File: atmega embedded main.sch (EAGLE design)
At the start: 144 parts, among them IC1 ATMEGA328PROUND, K100 SWITCH, K101 SWITCH, K102 SWITCH, K103 SWITCH, K104 SWITCH, K105 SWITCH, K106 SWITCH, K107 SWITCH, K108 SWITCH, K109 SWITCH, K110 SWITCH, K111 SWITCH, K112 SWITCH, K113 SWITCH, K114 SWITCH, K115 SWITCH, K116 SWITCH, K117 SWITCH, K118 SWITCH, K119 SWITCH, K120 SWITCH, K121 SWITCH, K122 SWITCH, K123 SWITCH, K124 SWITCH, K125 SWITCH, K126 SWITCH, K127 SWITCH, K128 SWITCH, K129 SWITCH, K130 SWITCH, K60 SWITCH, K67 SWITCH, K68 SWITCH, K69 SWITCH, K70 SWITCH, K71 SWITCH, K72 SWITCH, K73 SWITCH, K74 SWITCH, K75 SWITCH, K76 SWITCH, K77 SWITCH, K78 SWITCH, K79 SWITCH, K80 SWITCH, K81 SWITCH, K82 SWITCH, K83 SWITCH, K84 SWITCH, K85 SWITCH, K86 SWITCH, K87 SWITCH, K88 SWITCH, K89 SWITCH, K90 SWITCH, K91 SWITCH, K92 SWITCH, K93 SWITCH, K94 SWITCH, K95 SWITCH, K96 SWITCH, K97 SWITCH, K98 SWITCH, K99 SWITCH

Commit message: Compacted stuff around the chip
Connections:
- net N$21: now also IC1.(PCI18/INT0)PD2; no longer IC1.(PCI20/XCK/T0)PD4
- net ROW5: now also IC1.(PCI1/OC1A/OC1S)PB1; no longer IC1.(PCI2/SS/OC1B)PB2
- net ROW6: now also IC1.(PCI2/SS/OC1B)PB2; no longer IC1.(PCI1/OC1A/OC1S)PB1
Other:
- moved on the sheet: R7
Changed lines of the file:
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@@
 <attribute name="VALUE" x="243.84" y="96.774" size="1.778" layer="96"/>
 </instance>
-<instance part="R7" gate="G$1" x="241.3" y="93.98" smashed="yes">
-<attribute name="NAME" x="235.966" y="94.2086" size="1.778" layer="95"/>
-<attribute name="VALUE" x="243.84" y="94.234" size="1.778" layer="96"/>
+<instance part="R7" gate="G$1" x="241.3" y="99.06" smashed="yes">
+<attribute name="NAME" x="235.966" y="99.2886" size="1.778" layer="95"/>
+<attribute name="VALUE" x="243.84" y="99.314" size="1.778" layer="96"/>
 </instance>
 <instance part="K60" gate="G$1" x="68.58" y="35.56" rot="R180"/>
@@
 </segment>
 <segment>
-<pinref part="IC1" gate="G$1" pin="(PCI2/SS/OC1B)PB2"/>
-<wire x1="236.22" y1="76.2" x2="238.76" y2="76.2" width="0.1524" layer="91"/>
-<label x="238.76" y="76.2" size="1.778" layer="95"/>
+<pinref part="IC1" gate="G$1" pin="(PCI1/OC1A/OC1S)PB1"/>
+<wire x1="236.22" y1="78.74" x2="238.76" y2="78.74" width="0.1524" layer="91"/>
+<label x="238.76" y="78.74" size="1.778" layer="95"/>
 </segment>
 </net>
@@
 <segment>
 <pinref part="R7" gate="G$1" pin="2"/>
-<wire x1="246.38" y1="93.98" x2="248.92" y2="93.98" width="0.1524" layer="91"/>
-<label x="248.92" y="93.98" size="1.778" layer="95"/>
+<wire x1="246.38" y1="99.06" x2="248.92" y2="99.06" width="0.1524" layer="91"/>
+<label x="248.92" y="99.06" size="1.778" layer="95"/>
 </segment>
 </net>
@@
 </segment>
 <segment>
-<pinref part="IC1" gate="G$1" pin="(PCI1/OC1A/OC1S)PB1"/>
-<wire x1="236.22" y1="78.74" x2="238.76" y2="78.74" width="0.1524" layer="91"/>
-<label x="238.76" y="78.74" size="1.778" layer="95"/>
+<pinref part="IC1" gate="G$1" pin="(PCI2/SS/OC1B)PB2"/>
+<wire x1="236.22" y1="76.2" x2="238.76" y2="76.2" width="0.1524" layer="91"/>
+<label x="238.76" y="76.2" size="1.778" layer="95"/>
 </segment>
 </net>
@@
 </segment>
 </net>
-<net name="N$21" class="0">
-<segment>
-<pinref part="IC1" gate="G$1" pin="(PCI20/XCK/T0)PD4"/>
-<pinref part="R7" gate="G$1" pin="1"/>
-</segment>
-</net>
 <net name="N$68" class="0">
 <segment>
@@
 </segment>
 </net>
+<net name="N$21" class="0">
+<segment>
+<pinref part="IC1" gate="G$1" pin="(PCI18/INT0)PD2"/>
+<pinref part="R7" gate="G$1" pin="1"/>
+</segment>
+</net>

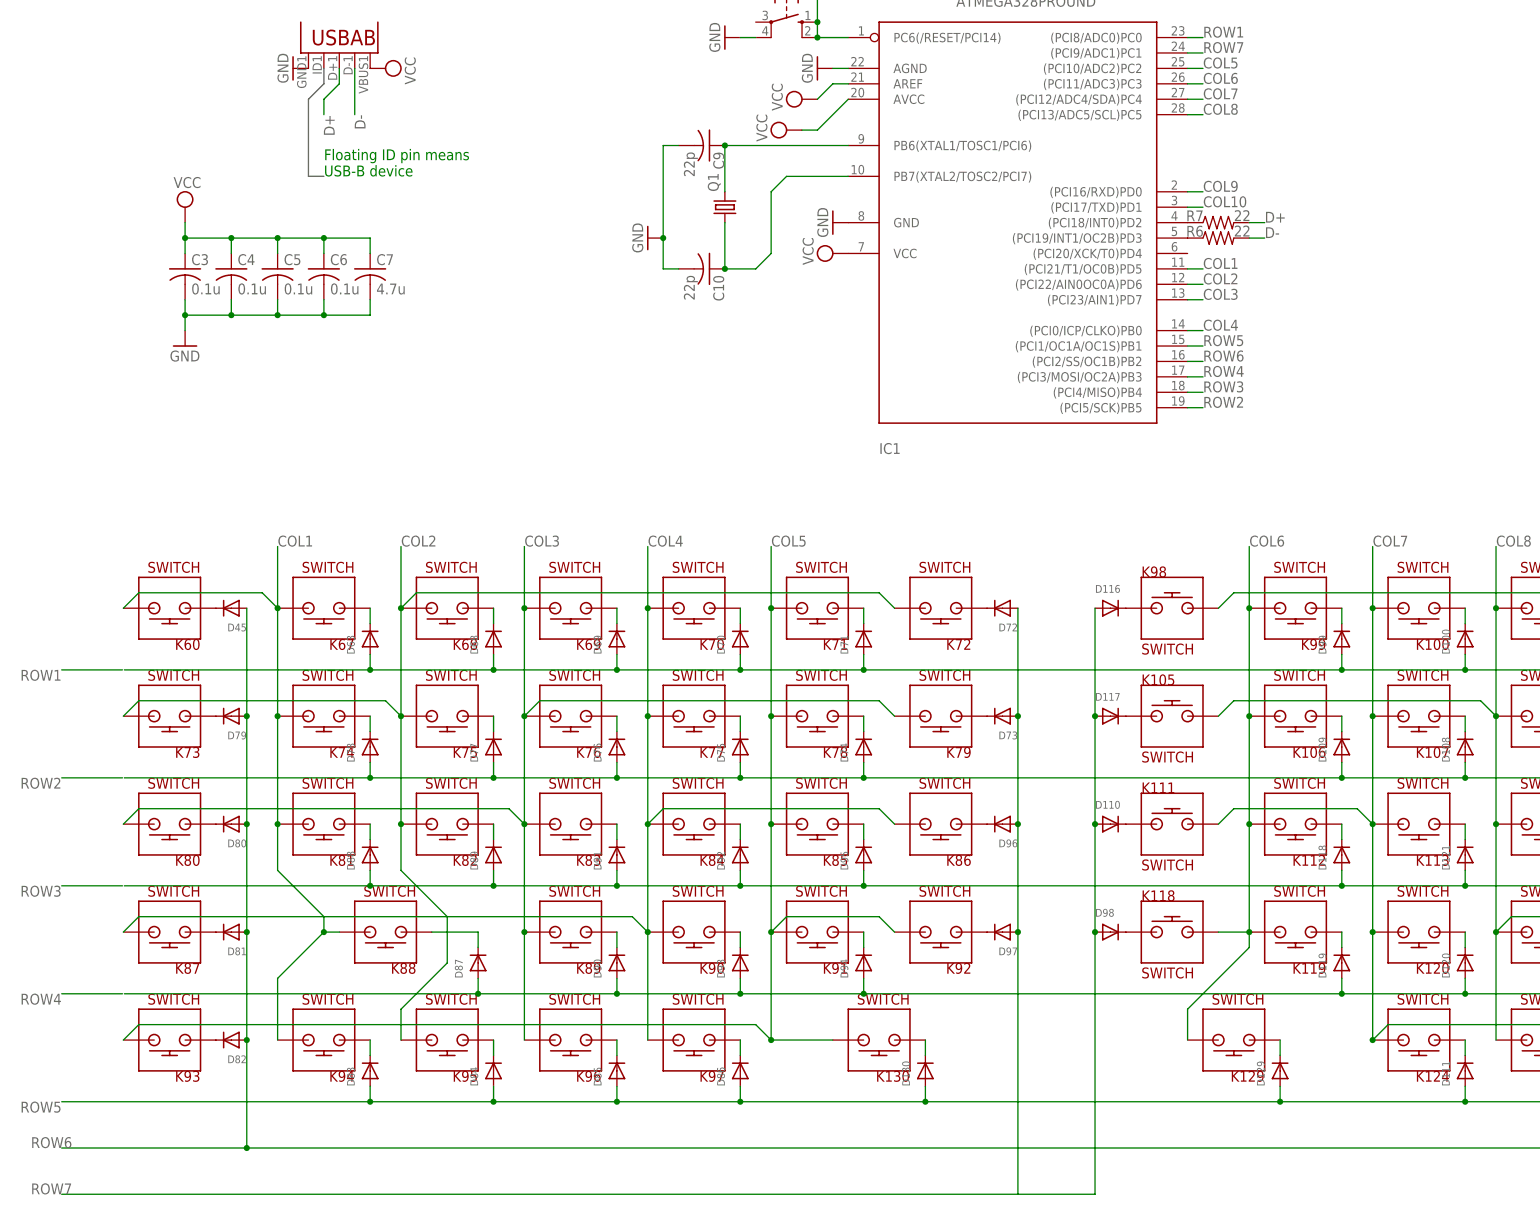
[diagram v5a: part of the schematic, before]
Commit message: Fixed errors and made adjustments for USB
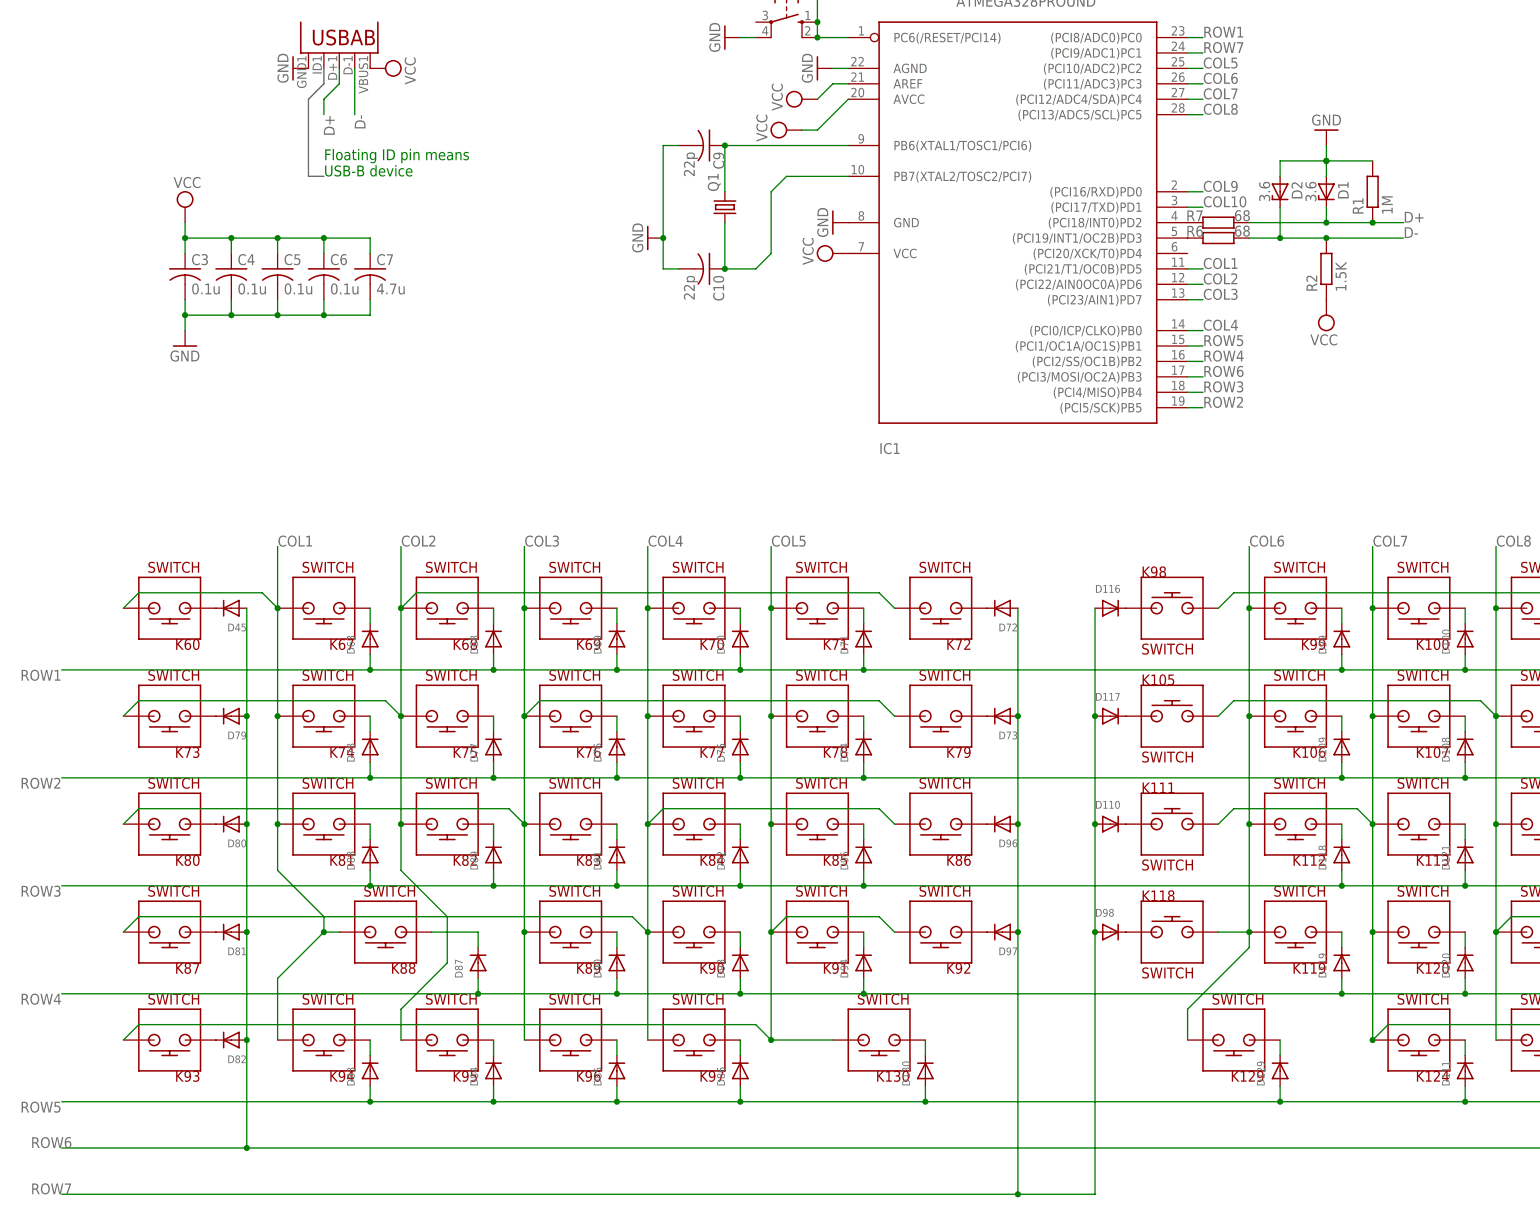
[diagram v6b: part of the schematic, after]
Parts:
- added D1, D2: 3.6, diode:ZENER-DIODESMB
- added R1: 1M, eagle-ltspice:RR1206
- added R2: 1.5K, eagle-ltspice:RR1206
- R6, R7: value 22 -> 68; device adafruit:R-US_M0805 -> eagle-ltspice:RR1206
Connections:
- net D+: now also D1.C, R1.1
- net D-: now also D2.C, R2.2
- net GND: now also D1.A, D2.A, R1.2
- net ROW4: now also IC1.(PCI2/SS/OC1B)PB2; no longer IC1.(PCI3/MOSI/OC2A)PB3
- net ROW6: now also IC1.(PCI3/MOSI/OC2A)PB3; no longer IC1.(PCI2/SS/OC1B)PB2
- net VCC: now also R2.1
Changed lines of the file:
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@@
 <part name="SUPPLY7" library="supply2" library_urn="urn:adsk.eagle:library:372" deviceset="VCC" device=""/>
 <part name="GND10" library="supply1" library_urn="urn:adsk.eagle:library:371" deviceset="GND" device=""/>
-<part name="R6" library="adafruit" deviceset="R-US_" device="M0805" value="22"/>
-<part name="R7" library="adafruit" deviceset="R-US_" device="M0805" value="22"/>
+<part name="R6" library="eagle-ltspice" library_urn="urn:adsk.eagle:library:217" deviceset="R" device="R1206" package3d_urn="urn:adsk.eagle:package:13301/1" value="68"/>
+<part name="R7" library="eagle-ltspice" library_urn="urn:adsk.eagle:library:217" deviceset="R" device="R1206" package3d_urn="urn:adsk.eagle:package:13301/1" value="68"/>
 <part name="K60" library="keyboard_switch" deviceset="SWITCH" device=""/>
 <part name="K67" library="keyboard_switch" deviceset="SWITCH" device=""/>
@@
 <part name="Q1" library="crystal" library_urn="urn:adsk.eagle:library:204" deviceset="CRYSTAL" device="HC49S" package3d_urn="urn:adsk.eagle:package:12071/1"/>
 <part name="S1" library="switch-omron" library_urn="urn:adsk.eagle:library:377" deviceset="10-XX" device="" package3d_urn="urn:adsk.eagle:package:27496/1"/>
+<part name="GND1" library="supply1" library_urn="urn:adsk.eagle:library:371" deviceset="GND" device=""/>
+<part name="D1" library="diode" library_urn="urn:adsk.eagle:library:210" deviceset="ZENER-DIODE" device="SMB" package3d_urn="urn:adsk.eagle:package:43404/2" value="3.6"/>
+<part name="D2" library="diode" library_urn="urn:adsk.eagle:library:210" deviceset="ZENER-DIODE" device="SMB" package3d_urn="urn:adsk.eagle:package:43404/2" value="3.6"/>
+<part name="R1" library="eagle-ltspice" library_urn="urn:adsk.eagle:library:217" deviceset="R" device="R1206" package3d_urn="urn:adsk.eagle:package:13301/1" value="1M"/>
+<part name="SUPPLY2" library="supply2" library_urn="urn:adsk.eagle:library:372" deviceset="VCC" device=""/>
+<part name="R2" library="eagle-ltspice" library_urn="urn:adsk.eagle:library:217" deviceset="R" device="R1206" package3d_urn="urn:adsk.eagle:package:13301/1" value="1.5K"/>
 </parts>
 <sheets>
@@
 <instance part="Q1" gate="G$1" x="160.02" y="101.6" rot="R90"/>
 <instance part="S1" gate="1" x="170.18" y="132.08" rot="R270"/>
+<instance part="GND1" gate="1" x="259.08" y="114.3" rot="R180"/>
+<instance part="D1" gate="G$1" x="259.08" y="104.14" rot="R270"/>
+<instance part="D2" gate="G$1" x="251.46" y="104.14" rot="R270"/>
+<instance part="R1" gate="G$1" x="266.7" y="104.14" rot="R90"/>
+<instance part="SUPPLY2" gate="G$1" x="259.08" y="83.82" rot="R180"/>
+<instance part="R2" gate="G$1" x="259.08" y="91.44" rot="R90"/>
 </instances>
 <busses>
@@
 <pinref part="GNDUSB" gate="1" pin="GND"/>
 </segment>
+<segment>
+<pinref part="D2" gate="G$1" pin="A"/>
+<wire x1="251.46" y1="106.68" x2="251.46" y2="109.22" width="0.1524" layer="91"/>
+<wire x1="251.46" y1="109.22" x2="259.08" y2="109.22" width="0.1524" layer="91"/>
+<pinref part="GND1" gate="1" pin="GND"/>
+<wire x1="259.08" y1="111.76" x2="259.08" y2="109.22" width="0.1524" layer="91"/>
+<pinref part="R1" gate="G$1" pin="2"/>
+<junction x="259.08" y="109.22"/>
+<pinref part="D1" gate="G$1" pin="A"/>
+<wire x1="259.08" y1="109.22" x2="266.7" y2="109.22" width="0.1524" layer="91"/>
+<wire x1="259.08" y1="109.22" x2="259.08" y2="106.68" width="0.1524" layer="91"/>
+<junction x="259.08" y="109.22"/>
+</segment>
 </net>
 <net name="VCC" class="0">
@@
 <pinref part="U1" gate="G$1" pin="VBUS"/>
 <pinref part="VCCUSB" gate="G$1" pin="VCC"/>
+</segment>
+<segment>
+<pinref part="R2" gate="G$1" pin="1"/>
+<pinref part="SUPPLY2" gate="G$1" pin="VCC"/>
 </segment>
 </net>
@@
 <net name="ROW4" class="0">
 <segment>
-<wire x1="50.8" y1="-27.94" x2="60.8076" y2="-27.94" width="0.1524" layer="91"/>
-<label x="50.8" y="-27.94" size="1.778" layer="95" rot="R180"/>
-</segment>
-<segment>
 <pinref part="D94" gate="G$1" pin="A"/>
 <wire x1="162.56" y1="-27.94" x2="182.88" y2="-27.94" width="0.1524" layer="91"/>
@@
 <wire x1="119.38" y1="-25.4" x2="119.38" y2="-27.94" width="0.1524" layer="91"/>
 <junction x="119.38" y="-27.94"/>
-<wire x1="61.1124" y1="-27.94" x2="119.38" y2="-27.94" width="0.1524" layer="91"/>
+<wire x1="50.8" y1="-27.94" x2="119.38" y2="-27.94" width="0.1524" layer="91"/>
 <wire x1="119.38" y1="-27.94" x2="142.24" y2="-27.94" width="0.1524" layer="91"/>
 <wire x1="142.24" y1="-27.94" x2="162.56" y2="-27.94" width="0.1524" layer="91"/>
@@
 <junction x="182.88" y="-27.94"/>
 <junction x="261.62" y="-27.94"/>
-</segment>
-<segment>
-<pinref part="IC1" gate="G$1" pin="(PCI3/MOSI/OC2A)PB3"/>
-<wire x1="236.22" y1="73.66" x2="238.76" y2="73.66" width="0.1524" layer="91"/>
-<label x="238.76" y="73.66" size="1.778" layer="95"/>
+<label x="50.8" y="-27.94" size="1.778" layer="95" rot="R180"/>
+</segment>
+<segment>
+<pinref part="IC1" gate="G$1" pin="(PCI2/SS/OC1B)PB2"/>
+<wire x1="236.22" y1="76.2" x2="238.76" y2="76.2" width="0.1524" layer="91"/>
+<label x="238.76" y="76.2" size="1.778" layer="95"/>
 </segment>
 </net>
@@
 <wire x1="162.56" y1="-7.62" x2="162.56" y2="-10.16" width="0.1524" layer="91"/>
 <junction x="162.56" y="-10.16"/>
-<wire x1="61.1124" y1="-10.16" x2="101.6" y2="-10.16" width="0.1524" layer="91"/>
 <pinref part="D124" gate="G$1" pin="A"/>
+<wire x1="50.8" y1="-10.16" x2="101.6" y2="-10.16" width="0.1524" layer="91"/>
 <wire x1="342.9" y1="-7.62" x2="342.9" y2="-10.16" width="0.1524" layer="91"/>
 <wire x1="322.58" y1="-10.16" x2="342.9" y2="-10.16" width="0.1524" layer="91"/>
@@
 <junction x="182.88" y="-10.16"/>
 <junction x="261.62" y="-10.16"/>
-</segment>
-<segment>
-<wire x1="50.8" y1="-10.16" x2="60.8076" y2="-10.16" width="0.1524" layer="91"/>
 <label x="50.8" y="-10.16" size="1.778" layer="95" rot="R180"/>
 </segment>
@@
 <wire x1="162.56" y1="10.16" x2="162.56" y2="7.62" width="0.1524" layer="91"/>
 <junction x="162.56" y="7.62"/>
-<wire x1="61.1124" y1="7.62" x2="101.6" y2="7.62" width="0.1524" layer="91"/>
 <pinref part="D105" gate="G$1" pin="A"/>
+<wire x1="50.8" y1="7.62" x2="101.6" y2="7.62" width="0.1524" layer="91"/>
 <wire x1="342.9" y1="10.16" x2="342.9" y2="7.62" width="0.1524" layer="91"/>
 <wire x1="322.58" y1="7.62" x2="342.9" y2="7.62" width="0.1524" layer="91"/>
@@
 <junction x="182.88" y="7.62"/>
 <junction x="261.62" y="7.62"/>
-</segment>
-<segment>
-<wire x1="50.8" y1="7.62" x2="60.8076" y2="7.62" width="0.1524" layer="91"/>
 <label x="50.8" y="7.62" size="1.778" layer="95" rot="R180"/>
 </segment>
@@
 <wire x1="101.6" y1="27.94" x2="101.6" y2="25.4" width="0.1524" layer="91"/>
 <junction x="101.6" y="25.4"/>
-<wire x1="61.1124" y1="25.4" x2="101.6" y2="25.4" width="0.1524" layer="91"/>
 <pinref part="D99" gate="G$1" pin="A"/>
+<wire x1="50.8" y1="25.4" x2="101.6" y2="25.4" width="0.1524" layer="91"/>
 <wire x1="261.62" y1="27.94" x2="261.62" y2="25.4" width="0.1524" layer="91"/>
 <wire x1="261.62" y1="25.4" x2="281.94" y2="25.4" width="0.1524" layer="91"/>
@@
 <junction x="182.88" y="25.4"/>
 <junction x="261.62" y="25.4"/>
-</segment>
-<segment>
-<wire x1="50.8" y1="25.4" x2="60.8076" y2="25.4" width="0.1524" layer="91"/>
 <label x="50.8" y="25.4" size="1.778" layer="95" rot="R180"/>
 </segment>
@@
 </segment>
 <segment>
+<label x="271.78" y="99.06" size="1.778" layer="95"/>
+<pinref part="R1" gate="G$1" pin="1"/>
+<wire x1="266.7" y1="99.06" x2="271.78" y2="99.06" width="0.1524" layer="91"/>
 <pinref part="R7" gate="G$1" pin="2"/>
-<wire x1="246.38" y1="99.06" x2="248.92" y2="99.06" width="0.1524" layer="91"/>
-<label x="248.92" y="99.06" size="1.778" layer="95"/>
+<wire x1="246.38" y1="99.06" x2="259.08" y2="99.06" width="0.1524" layer="91"/>
+<junction x="266.7" y="99.06"/>
+<pinref part="D1" gate="G$1" pin="C"/>
+<wire x1="259.08" y1="99.06" x2="266.7" y2="99.06" width="0.1524" layer="91"/>
+<wire x1="259.08" y1="101.6" x2="259.08" y2="99.06" width="0.1524" layer="91"/>
+<junction x="259.08" y="99.06"/>
 </segment>
 </net>
@@
 </segment>
 <segment>
+<label x="271.78" y="96.52" size="1.778" layer="95"/>
+<pinref part="R2" gate="G$1" pin="2"/>
+<wire x1="259.08" y1="96.52" x2="271.78" y2="96.52" width="0.1524" layer="91"/>
 <pinref part="R6" gate="G$1" pin="2"/>
-<wire x1="246.38" y1="96.52" x2="248.92" y2="96.52" width="0.1524" layer="91"/>
-<label x="248.92" y="96.52" size="1.778" layer="95"/>
+<wire x1="246.38" y1="96.52" x2="251.46" y2="96.52" width="0.1524" layer="91"/>
+<junction x="259.08" y="96.52"/>
+<pinref part="D2" gate="G$1" pin="C"/>
+<wire x1="251.46" y1="96.52" x2="259.08" y2="96.52" width="0.1524" layer="91"/>
+<wire x1="251.46" y1="101.6" x2="251.46" y2="96.52" width="0.1524" layer="91"/>
+<junction x="251.46" y="96.52"/>
 </segment>
 </net>
@@
 </segment>
 <segment>
-<pinref part="IC1" gate="G$1" pin="(PCI2/SS/OC1B)PB2"/>
-<wire x1="236.22" y1="76.2" x2="238.76" y2="76.2" width="0.1524" layer="91"/>
-<label x="238.76" y="76.2" size="1.778" layer="95"/>
+<pinref part="IC1" gate="G$1" pin="(PCI3/MOSI/OC2A)PB3"/>
+<wire x1="236.22" y1="73.66" x2="238.76" y2="73.66" width="0.1524" layer="91"/>
+<label x="238.76" y="73.66" size="1.778" layer="95"/>
 </segment>
 </net>
@@
 <wire x1="220.98" y1="17.78" x2="220.98" y2="35.56" width="0.1524" layer="91"/>
 <junction x="220.98" y="17.78"/>
+<junction x="208.28" y="-60.96"/>
 </segment>
 <segment>
@@
 </sheet>
 </sheets>
+<errors>
+</errors>
 </schematic>
 </drawing>
